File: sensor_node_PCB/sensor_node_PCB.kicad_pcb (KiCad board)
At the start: 2 copper layers, 102.6 x 49 mm, 51 parts, among them J1 USB_B_Mini, J2 INPUT CONNECTOR, J3 OUTPUT_CONNECTOR, P1 BREAKOUTS, Q1 FDN340P, Q2 BSS138, Q3 BSS138, SW1 RESET_SWITCH, U1 LMV358IDGKR, U2 LD1117S50TR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

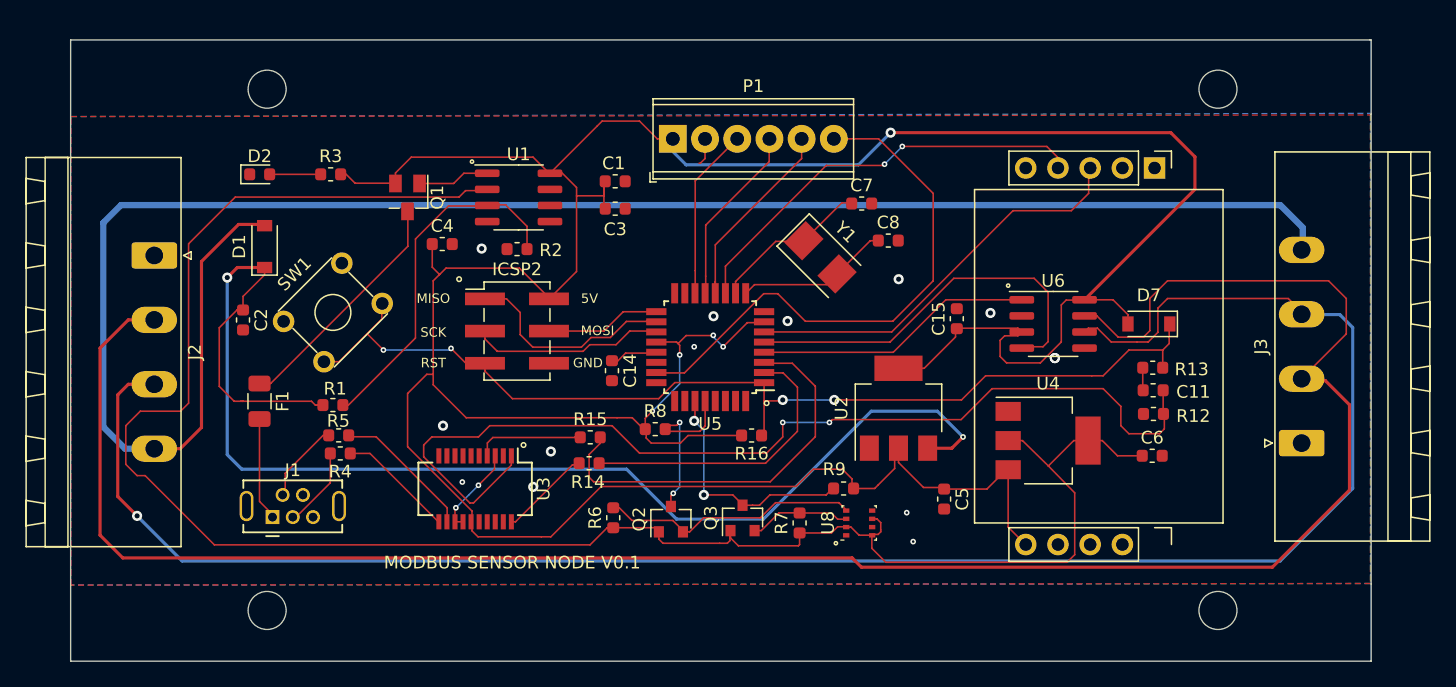
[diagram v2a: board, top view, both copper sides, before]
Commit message: cleaned up drc violations
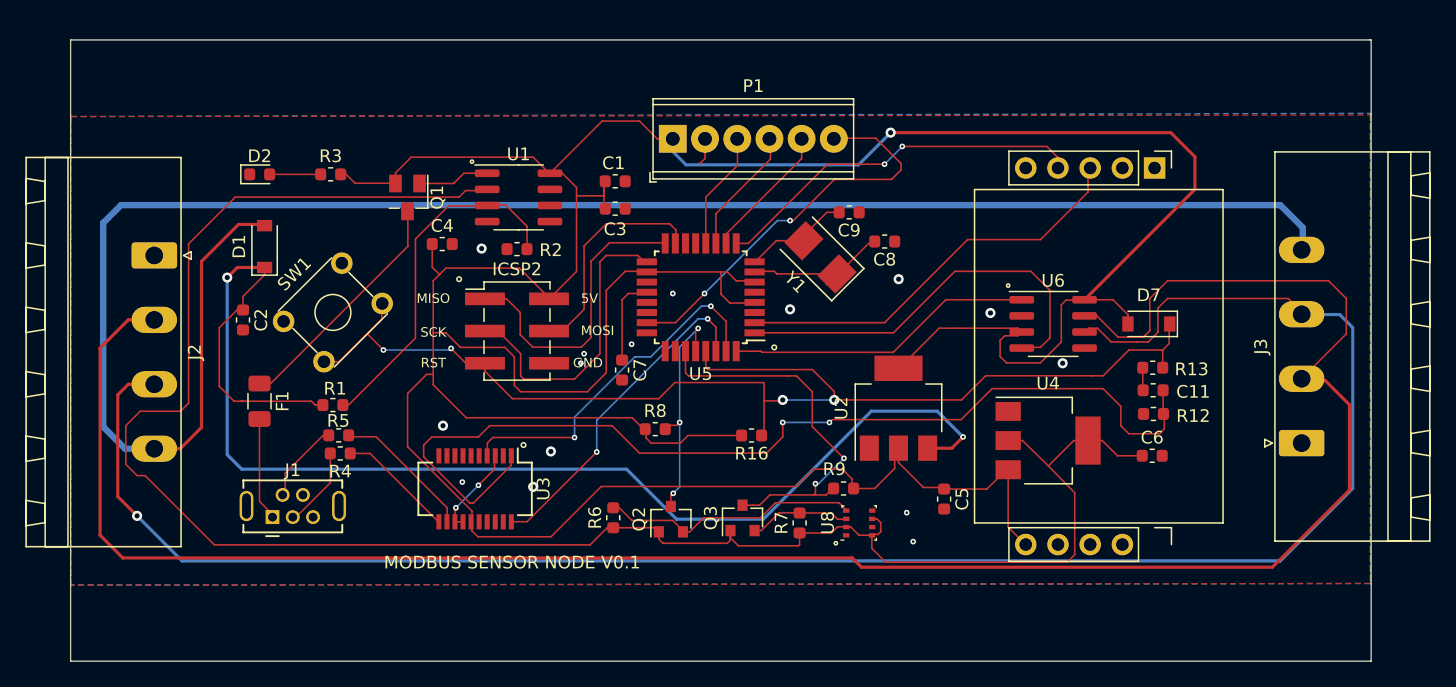
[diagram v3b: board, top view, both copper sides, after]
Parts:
- removed C14, C15: 0.1 uF, Capacitor_SMD:C_0603_1608Metric
- removed R14, R15: 1K, Resistor_SMD:R_0603_1608Metric
- removed REF** (x4): MountingHole_3mm, MountingHole:MountingHole_3mm
- added C9: 18pF, Capacitor_SMD:C_0603_1608Metric, F.Cu at (158.9, 97.6)
- C7: value 18pF -> 0.1 uF
- U5: value ATMEGA328P -> ATmega328P-AU
- moved C7 23.0 mm to (141.0, 110.0), turned to 270 degrees
- moved U5 4.00 mm to (147.2, 104.3)
- moved C8 0.29 mm to (161.7, 99.9), turned to 180 degrees
- turned Y1 to 135 degrees
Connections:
- net /atmega328p/ARD_AN1 renamed Net-(U5-Pad24)
- net /atmega328p/ARD_AN2 renamed Net-(U5-Pad25)
- net /atmega328p/ARD_AN3 renamed Net-(U5-Pad26)
- C8 pad 1: Net-(C8-Pad1) -> GND
- C8 pad 2: GND -> Net-(C8-Pad2)
- D7 pad 1: /atmega328p/328P_RESET -> /atmega328p/RESET
- ICSP2 pad 5: /atmega328p/328P_RESET -> /atmega328p/RESET
- R13 pad 2: /atmega328p/328P_RESET -> /atmega328p/RESET
- R16 pad 1: /atmega328p/328P_RESET -> /atmega328p/RESET
- SW1 pad 3: /atmega328p/328P_RESET -> /atmega328p/RESET
- SW1 pad 4: /atmega328p/328P_RESET -> /atmega328p/RESET
- U5 pad 1: /atmega328p/328P_RESET -> /ARD_TX1
- U5 pad 10: Net-(C7-Pad1) -> /atmega328p/ARD_DIG6
- U5 pad 11: /ARD_TX2 -> /atmega328p/ARD_DIG7
- U5 pad 12: /atmega328p/ARD_DIG6 -> /atmega328p/ARD_DIG8
- U5 pad 13: /atmega328p/ARD_DIG7 -> Net-(U5-Pad13)
- U5 pad 14: /atmega328p/ARD_DIG8 -> Net-(U5-Pad14)
- U5 pad 15: /atmega328p/ARD_DIG9 -> 328P_ICSP_MOSI
- U5 pad 16: /atmega328p/ARD_DIG10/SPI_SS -> 328P_ICSP_MISO
- U5 pad 17: 328P_ICSP_MOSI -> 328P_ICSP_SCK
- U5 pad 18: 328P_ICSP_MISO -> 5V_LDO
- U5 pad 19: 328P_ICSP_SCK -> Net-(U5-Pad19)
- U5 pad 2: /atmega328p/ARD_DIG0 -> /ARD_RX2
- U5 pad 20: 5V_LDO -> Net-(C7-Pad1)
- U5 pad 21: /atmega328p/AREF -> GND
- U5 pad 22: GND -> Net-(U5-Pad22)
- U5 pad 29: (no net) -> /atmega328p/RESET
- U5 pad 3: /atmega328p/ARD_DIG1 -> GND
- U5 pad 30: (no net) -> /ard_rx
- U5 pad 31: (no net) -> /ard_tx
- U5 pad 32: (no net) -> /ARD_RX1
- U5 pad 4: /ARD_RX1 -> 5V_LDO
- U5 pad 5: /ARD_TX1 -> GND
- U5 pad 6: /ARD_RX2 -> 5V_LDO
- U5 pad 7: 5V_LDO -> Net-(C8-Pad2)
- U5 pad 8: GND -> Net-(C9-Pad2)
- U5 pad 9: Net-(C8-Pad1) -> /ARD_TX2
- Y1 pad 1: Net-(C7-Pad1) -> Net-(C8-Pad2)
- Y1 pad 2: Net-(C8-Pad1) -> Net-(C9-Pad2)
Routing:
- net /atmega328p/RESET: track 0.00 -> 95.3 mm, vias 0 -> 4
- net /atmega328p/328P_RESET: track 82.6 -> 0.00 mm, vias 4 -> 0
- net /atmega328p/ARD_DIG1: track 31.7 -> 0.00 mm
- net 5V_LDO: track 275.3 -> 298.8 mm, vias 5 -> 1
- net /atmega328p/ARD_DIG0: track 23.2 -> 0.00 mm
- net /ard_tx: track 8.50 -> 28.1 mm, vias 0 -> 2
- net /ard_rx: track 7.03 -> 26.4 mm, vias 0 -> 2
- net Net-(C8-Pad1): track 12.1 -> 0.00 mm
- net Net-(C8-Pad2): track 0.00 -> 11.7 mm
- net /atmega328p/ARD_AN0: track 43.3 -> 31.6 mm, vias 0 -> 2
- net /ARD_SDA: track 18.8 -> 30.3 mm
- net 328P_ICSP_MOSI: track 9.28 -> 17.7 mm
- net 328P_ICSP_SCK: track 15.4 -> 23.7 mm
- net Net-(C9-Pad2): track 0.00 -> 8.19 mm
- net Net-(C7-Pad1): track 12.5 -> 7.24 mm
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
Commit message: removed 2nd connector - fixed mounting holes
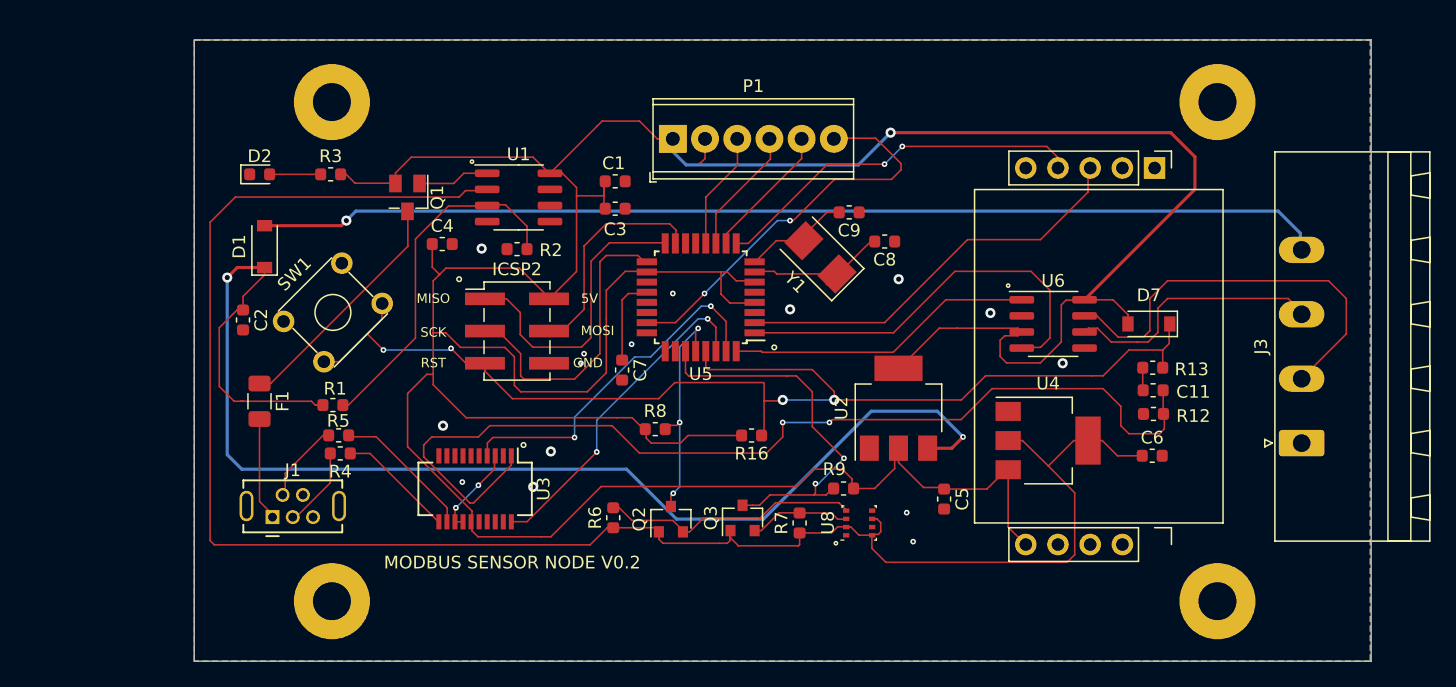
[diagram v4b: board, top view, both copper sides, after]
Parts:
- removed J2: INPUT CONNECTOR, Connector_Phoenix_MSTB:PhoenixContact_MSTB_2,5_4-GF-5,08_1x04_P5.08mm_Horizontal_ThreadedFlange
- added REF**: MountingHole_3mm_Pad, MountingHole:MountingHole_3mm_Pad, F.Cu at (118.1, 128.3)
- added REF**: MountingHole_3mm_Pad, MountingHole:MountingHole_3mm_Pad, F.Cu at (188.0, 128.3)
- added REF**: MountingHole_3mm_Pad, MountingHole:MountingHole_3mm_Pad, F.Cu at (188.0, 88.9)
- added REF**: MountingHole_3mm_Pad, MountingHole:MountingHole_3mm_Pad, F.Cu at (118.1, 88.9)
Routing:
- net /MODBUS_B+: track 166.5 -> 33.1 mm
- net /MODBUS_A-: track 151.0 -> 20.8 mm, vias 1 -> 0
- net 12V_BUS: track 142.3 -> 83.9 mm, vias 0 -> 1
- net 3V3_LDO: track 152.8 -> 145.1 mm
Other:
- board size 102.6 x 49 mm -> 92.8 x 49 mm
- board text added: "MODBUS SENSOR NODE V0.2"
- board text removed: "MODBUS SENSOR NODE V0.1"
